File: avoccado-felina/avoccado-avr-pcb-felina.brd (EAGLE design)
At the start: 25 x 25 mm, 61 parts, among them Q1 16MHz, Q2 FET, U2 MCP73831

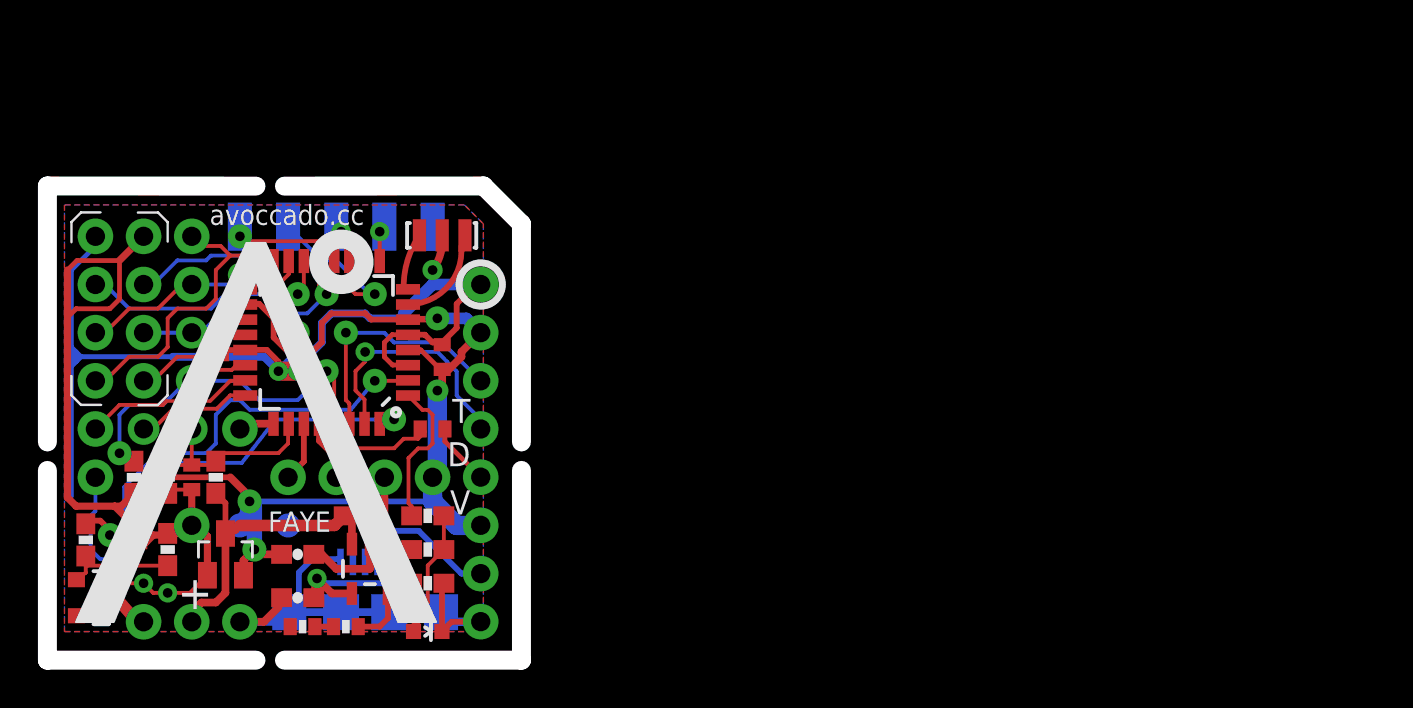
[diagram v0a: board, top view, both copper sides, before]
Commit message: Faye: adjusted Rs, new PCB: Felina
Felina is a larger PCB with the MPU6050 on board instead of a breakout
board.
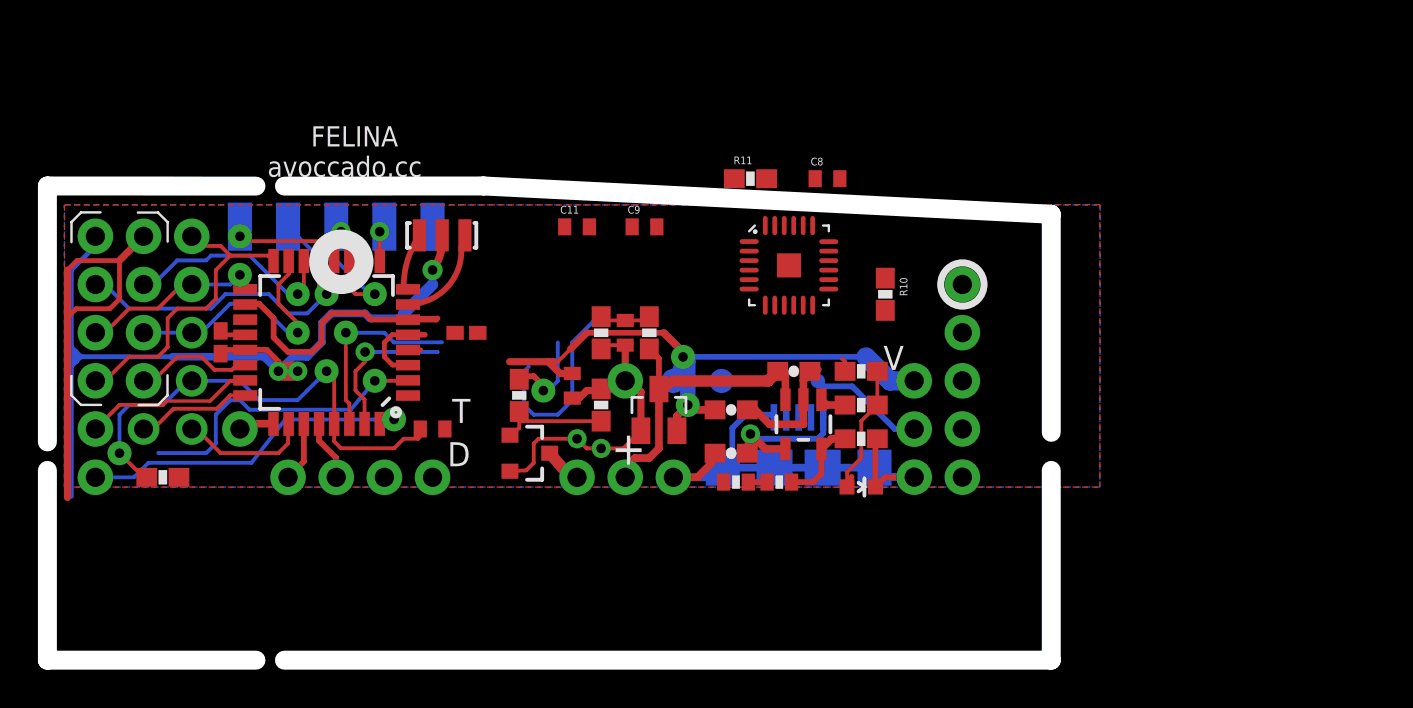
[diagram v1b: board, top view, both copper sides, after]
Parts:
- added C11, C8: 0.1uF, SparkFun:C0402
- added C9: 2.2nF, SparkFun:C0402
- added R10, R11: 10K, SparkFun-Resistors:0603-RES
- added U1: MPU-6000QFN-24, SparkFun-Sensors:QFN-24-TESTING
- C1, C3: device SparkFun:C0402 -> resistor:C0402K
- moved JP10 25.4 mm to (47.8, 9.15)
- moved JP11 25.4 mm to (47.8, 16.8)
- moved JP3 25.4 mm to (47.8, 19.3)
- moved JP8 25.4 mm to (47.8, 14.2)
- moved JP9 25.4 mm to (47.8, 11.7)
- moved C4 24.1 mm to (35.6, 10.4)
- moved C5 24.1 mm to (38.9, 14.7)
- moved C6 24.1 mm to (35.6, 12.7)
- moved JP17 24.1 mm to (45.2, 11.7)
- moved JP18 24.1 mm to (45.2, 14.2)
- moved JP26 24.1 mm to (45.2, 9.15)
- moved R5 24.1 mm to (28.7, 13.0)
- moved R7 24.1 mm to (28.7, 16.8)
- moved C10 24.1 mm to (27.2, 14.0)
- moved C7 24.1 mm to (30.0, 16.8)
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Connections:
- removed net D2: MCU.32, TP2.1
- new net D2-INT: MCU.32, TP2.1, U1.12
- new net N$10: C11.1, U1.8
- new net N$4: R10.1, U1.23
- new net N$5: R11.1, U1.24
- new net N$7: C8.1, U1.10
- new net N$8: C9.1, U1.20
- net 3.3V: now also R10.2, R11.2, U1.13
- net GND: now also C11.2, C8.2, C9.2, U1.1, U1.11, U1.18, U1.9
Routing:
- net D2-INT: track 0.00 -> 28.1 mm, vias 0 -> 1
- net D2: track 26.0 -> 0.00 mm, vias 1 -> 0
- net 3.3V: track 85.0 -> 70.0 mm, vias 4 -> 2
- net GND: track 112.5 -> 103.0 mm
- net D3: track 8.43 -> 1.22 mm
- net TXO: track 13.2 -> 9.05 mm
- net DTR: track 3.33 -> 0.01 mm
- net RXI: track 13.1 -> 10.2 mm
- net D4: track 23.5 -> 21.0 mm
- net RESET: track 25.1 -> 26.2 mm
- net A3: track 10.4 -> 9.84 mm
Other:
- board size 25 x 25 mm -> 52.9 x 25 mm
- board text added: "FELINA"
- board text removed: "FAYE"

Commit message: Felina: rearrange and start to route
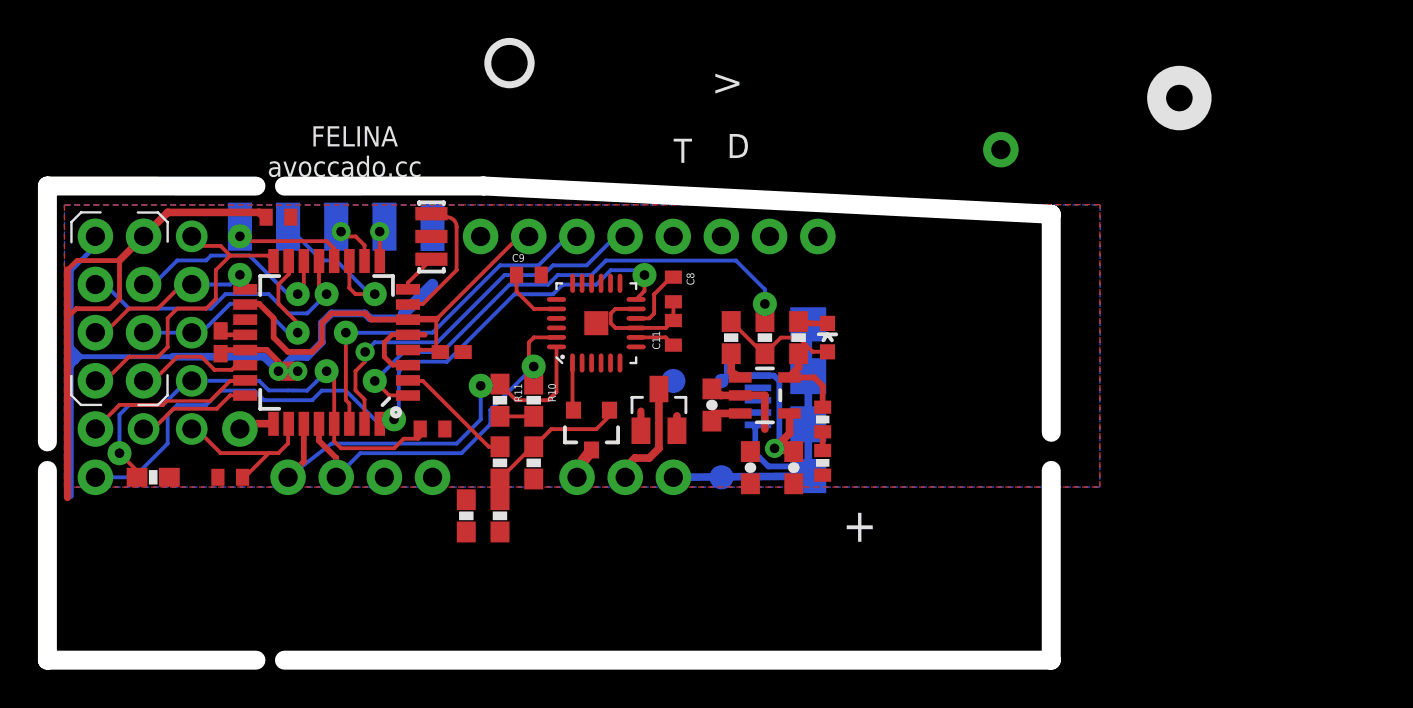
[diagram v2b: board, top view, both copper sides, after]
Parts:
- JP12: value M01PTH -> M01NOSILK-KIT; device SparkFun-Connectors:1X01 -> SparkFun-Connectors:1X01NS-KIT
- moved JP3 25.5 mm to (22.3, 21.8), turned to 90 degrees
- moved JP11 23.4 mm to (24.9, 21.8), turned to 90 degrees
- moved JP6 23.3 mm to (49.8, 26.4)
- moved C7 22.2 mm to (9.14, 9.14), turned to 180 degrees
- moved JP8 21.7 mm to (27.4, 21.8), turned to 90 degrees
- moved JP9 20.5 mm to (30.0, 21.8), turned to 90 degrees
- moved JP10 19.8 mm to (32.5, 21.8), turned to 90 degrees
- moved R10 19.4 mm to (25.1, 13.2)
- moved C10 17.9 mm to (11.7, 22.9), turned to 0 degrees
- moved R11 17.6 mm to (23.4, 13.2), turned to 270 degrees
- moved JP26 14.8 mm to (37.6, 21.8), turned to 90 degrees
- moved R8 13.6 mm to (21.6, 7.11)
- moved JP18 12.7 mm to (35.0, 21.8), turned to 90 degrees
- moved JP17 11.4 mm to (40.1, 21.8), turned to 90 degrees
- moved R7 11.0 mm to (23.4, 7.11)
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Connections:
- removed net N$4: R10.1, U1.23
- removed net N$5: R11.1, U1.24
- net A4: now also R11.1, U1.24
- net A5: now also R10.1, U1.23
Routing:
- net D3: track 1.22 -> 27.6 mm, vias 0 -> 2
- net A4: track 3.17 -> 23.2 mm, vias 0 -> 1
- net A5: track 3.20 -> 21.4 mm, vias 0 -> 1
- net GND: track 103.0 -> 85.7 mm, vias 5 -> 2
- net D4: track 21.0 -> 6.30 mm, vias 2 -> 0
- net 3.3V: track 70.0 -> 57.2 mm, vias 2 -> 0
- net D2-INT: track 28.1 -> 39.8 mm, vias 1 -> 2
- net TXO: track 9.05 -> 20.4 mm
- net RXI: track 10.2 -> 19.2 mm
- net VBAT: track 16.9 -> 7.89 mm
- net 5V: track 16.1 -> 12.0 mm
- net N$7: track 0.00 -> 3.46 mm
- net N$8: track 0.00 -> 3.36 mm
- net N$2: track 4.88 -> 7.22 mm
- net N$10: track 0.00 -> 2.13 mm
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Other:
- board text removed: "A1"
- board text removed: "A3"

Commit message: route 3V3
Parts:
- moved C2 15.9 mm to (33.9, 19.1), turned to 90 degrees
- moved C10 13.4 mm to (24.6, 19.3), turned to 270 degrees
- moved JP18 9.86 mm to (44.7, 23.9)
- moved R7 6.28 mm to (21.8, 13.2), turned to 270 degrees
- moved R8 2.81 mm to (21.8, 9.91)
- moved C9 2.65 mm to (24.1, 17.3), turned to 180 degrees
- moved JP17 2.54 mm to (40.1, 19.3)
- moved JP26 1.52 mm to (36.1, 21.8)
- moved C3 1.04 mm to (21.1, 16.8), turned to 270 degrees
- moved R1 0.25 mm to (23.6, 9.91)
- moved R11 0.25 mm to (23.6, 13.2)
- moved R10 0.25 mm to (25.4, 13.2)
- moved R5 0.25 mm to (25.4, 9.91)
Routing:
- net 3.3V: track 57.2 -> 87.5 mm, vias 0 -> 1
- net RESET: track 25.9 -> 51.9 mm, vias 2 -> 4
- net DTR: track 0.00 -> 2.72 mm
- net A3: track 8.78 -> 11.2 mm, vias 0 -> 1
- net GND: track 85.7 -> 87.9 mm
- net A4: track 23.2 -> 24.7 mm
- net D4: track 6.30 -> 7.82 mm
- net N$8: track 3.36 -> 1.88 mm
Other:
- board size 52.9 x 25 mm -> 42 x 17.4 mm

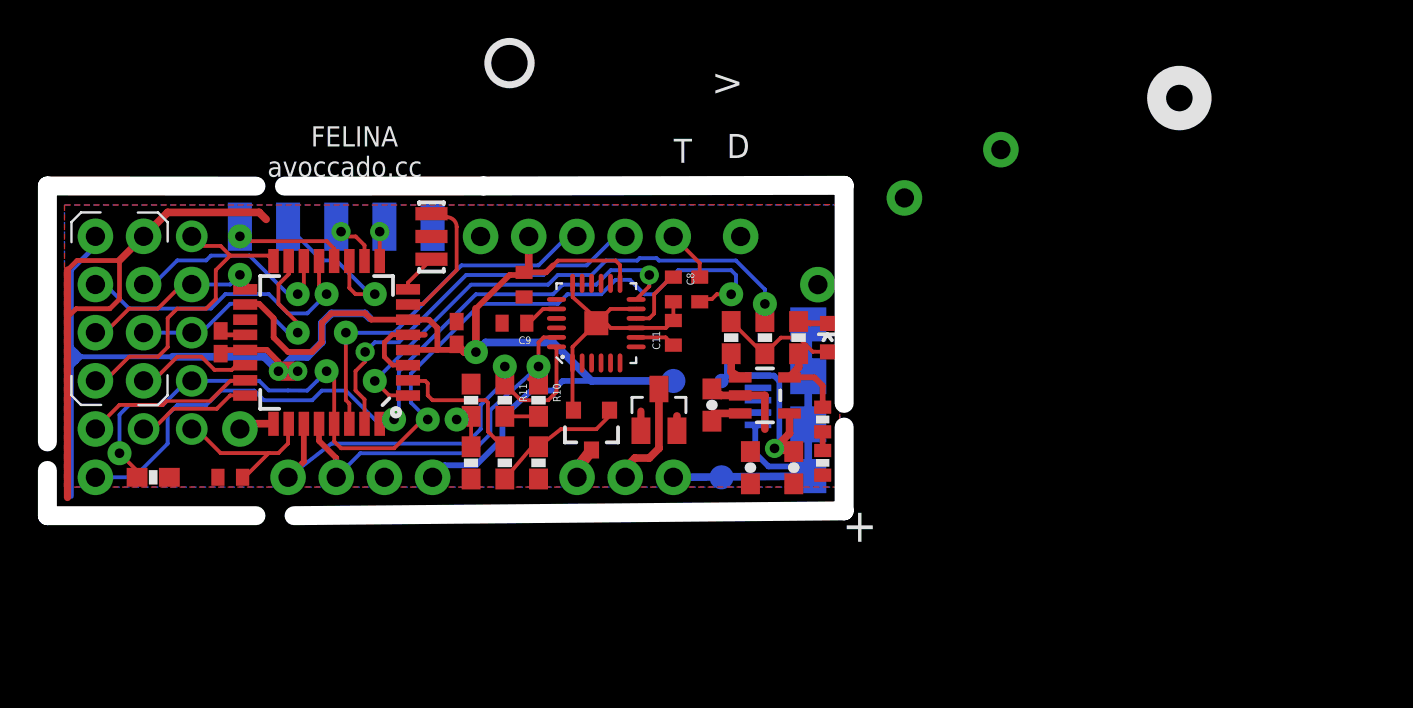
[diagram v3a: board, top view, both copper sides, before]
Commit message: move RST pullup away from bottom left
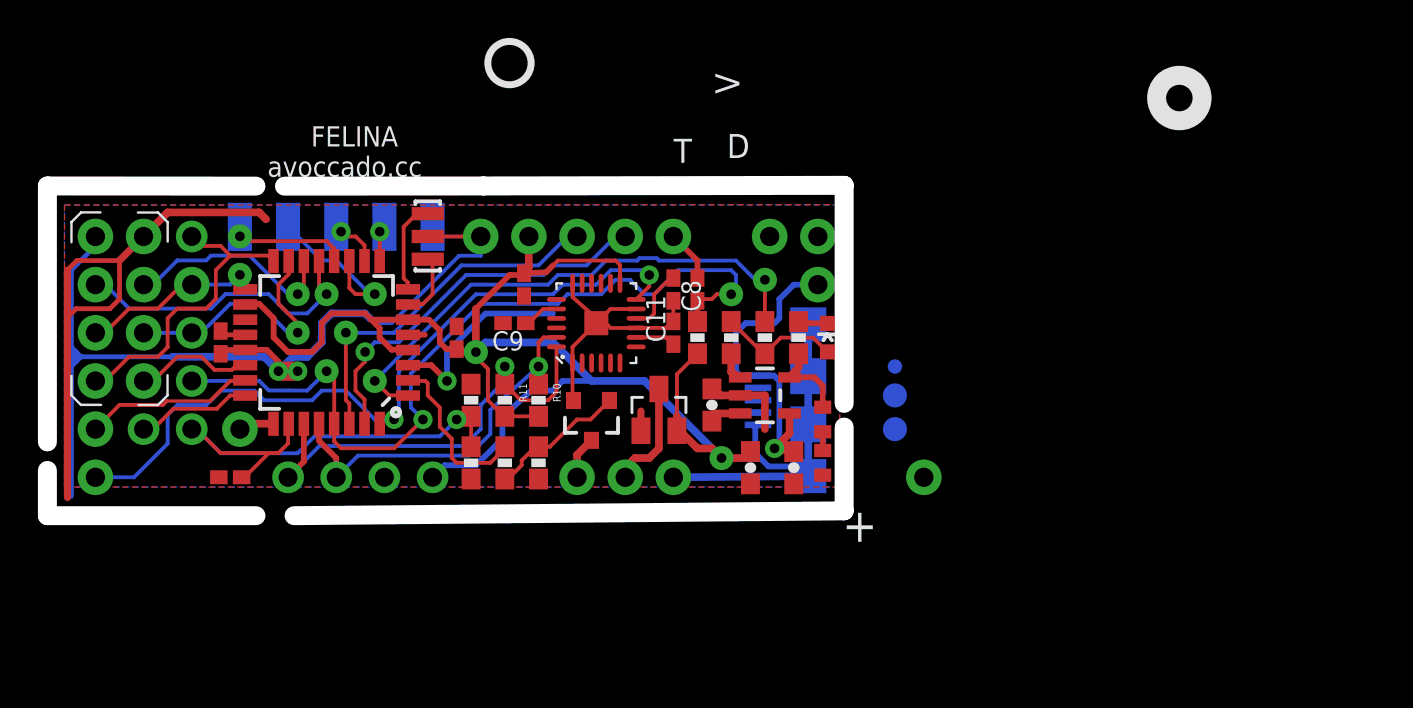
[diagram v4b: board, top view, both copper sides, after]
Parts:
- removed JP4, JP5: M021X02_NO_SILK, SparkFun-Connectors:1X02_NO_SILK
- added JP1, JP16, JP30, JP31: M01NOSILK-KIT, SparkFun-Connectors:1X01NS-KIT
- C10, C11, C2, C7, C8, C9: device SparkFun:C0402 -> rcl:C0402K
- R12, R9: device SparkFun-Resistors:0402-RES -> rcl:R0402
- R3: value RP -> 2K
- R4: value 1K -> 2K
- moved R2 29.6 mm to (33.8, 16.5), turned to 270 degrees
- moved JP18 14.8 mm to (45.7, 9.14)
- moved JP6 13.0 mm to (37.6, 21.8)
- moved TP5 11.7 mm to (44.2, 13.5)
- moved TP3 9.49 mm to (44.2, 11.7)
- moved TP4 9.18 mm to (44.2, 15.0)
- moved JP26 4.07 mm to (40.1, 21.8)
- moved Q2 0.51 mm to (28.2, 12.2)
- moved C3 0.25 mm to (21.1, 16.5)
- moved Q1 0.20 mm to (19.6, 21.8), turned to 270 degrees
- moved C2 0.12 mm to (33.8, 19.1)
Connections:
- net 3.3V: now also JP1.1; no longer JP4.1
- net A4: now also JP31.1; no longer JP5.2
- net A5: now also JP30.1; no longer JP5.1
- net GND: now also JP16.1; no longer JP4.2
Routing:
- net GND: track 87.9 -> 107.7 mm, vias 2 -> 3
- net 3.3V: track 87.5 -> 104.9 mm, vias 1 -> 2
- net A3: track 11.2 -> 26.5 mm
- net RESET: track 51.9 -> 44.0 mm, vias 4 -> 3
- net 5V: track 12.0 -> 17.6 mm
- net N$2: track 7.22 -> 3.47 mm
- net N$1: track 2.10 -> 4.95 mm
- net D4: track 7.82 -> 8.96 mm
- net D3: track 27.7 -> 28.7 mm
- net A5: track 21.0 -> 20.5 mm

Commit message: Vcc and GND routed at bottom
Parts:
- added JP4, JP5: M01NOSILK-KIT, SparkFun-Connectors:1X01NS-KIT
- added TP10: TPTP20R, testpad:TP20R
- moved JP18 16.6 mm to (35.1, 21.8)
- moved JP22 9.35 mm to (14.0, 5.33)
- moved TP3 4.75 mm to (45.5, 16.3)
- moved C7 4.47 mm to (4.70, 8.64), turned to 0 degrees
- moved TP4 4.38 mm to (43.4, 19.3)
- moved JP26 4.07 mm to (44.2, 21.6)
- moved JP17 2.54 mm to (40.1, 21.8)
- moved C10 2.18 mm to (22.9, 18.0), turned to 90 degrees
- moved C3 1.52 mm to (21.1, 18.0)
- moved TP5 1.02 mm to (45.2, 13.5)
- moved C9 0.92 mm to (24.6, 18.0), turned to 90 degrees
- moved Q2 0.57 mm to (27.9, 11.7)
- moved C11 0.25 mm to (32.5, 16.5)
- turned R5 to 270 degrees
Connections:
- net 3.3V: now also JP4.1
- net GND: now also JP5.1
- net VBAT: now also TP10.TP
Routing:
- net GND: track 107.7 -> 187.2 mm, vias 3 -> 6
- net 3.3V: track 104.9 -> 154.1 mm
- net VBAT: track 7.89 -> 14.7 mm
- net RESET: track 44.0 -> 41.4 mm
- net 5V: track 17.6 -> 20.0 mm
- net VIBR: track 2.26 -> 1.65 mm
- net A3: track 26.5 -> 26.7 mm, vias 1 -> 2

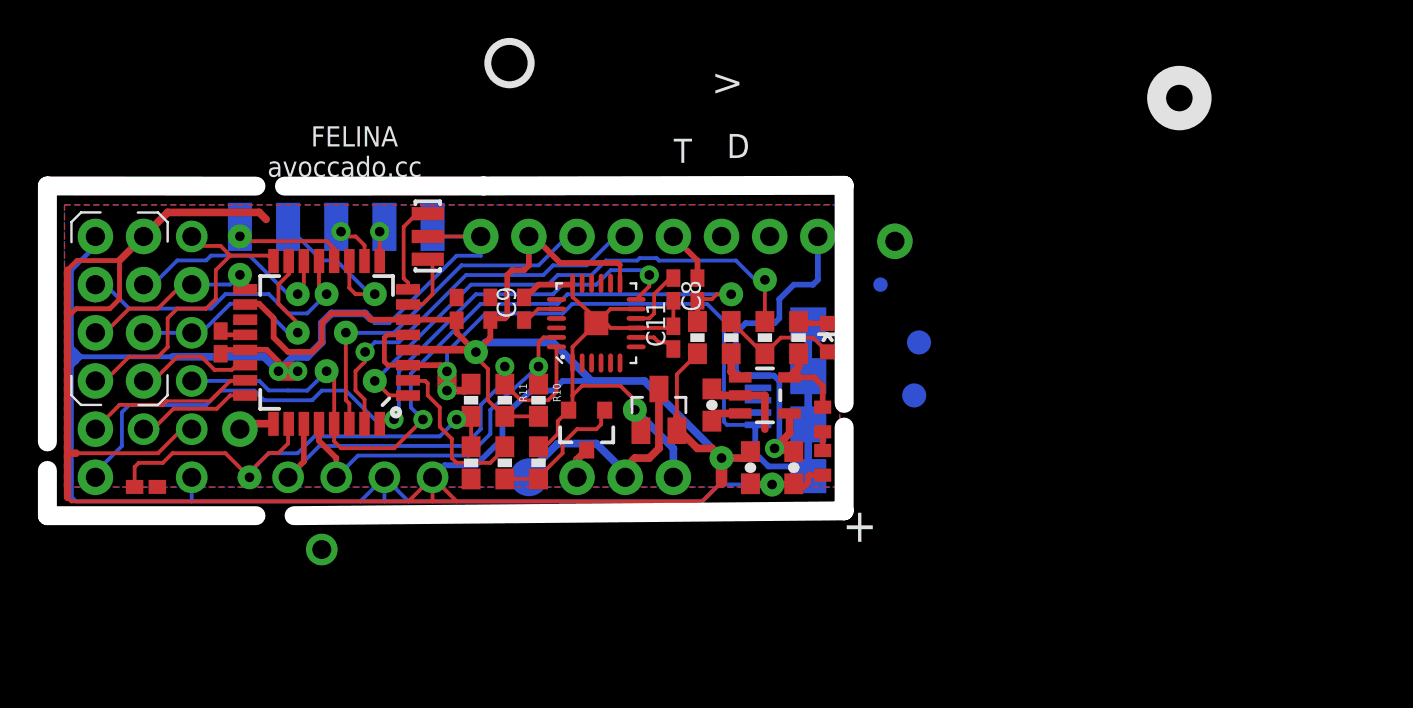
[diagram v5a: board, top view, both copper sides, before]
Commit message: route reset pullup
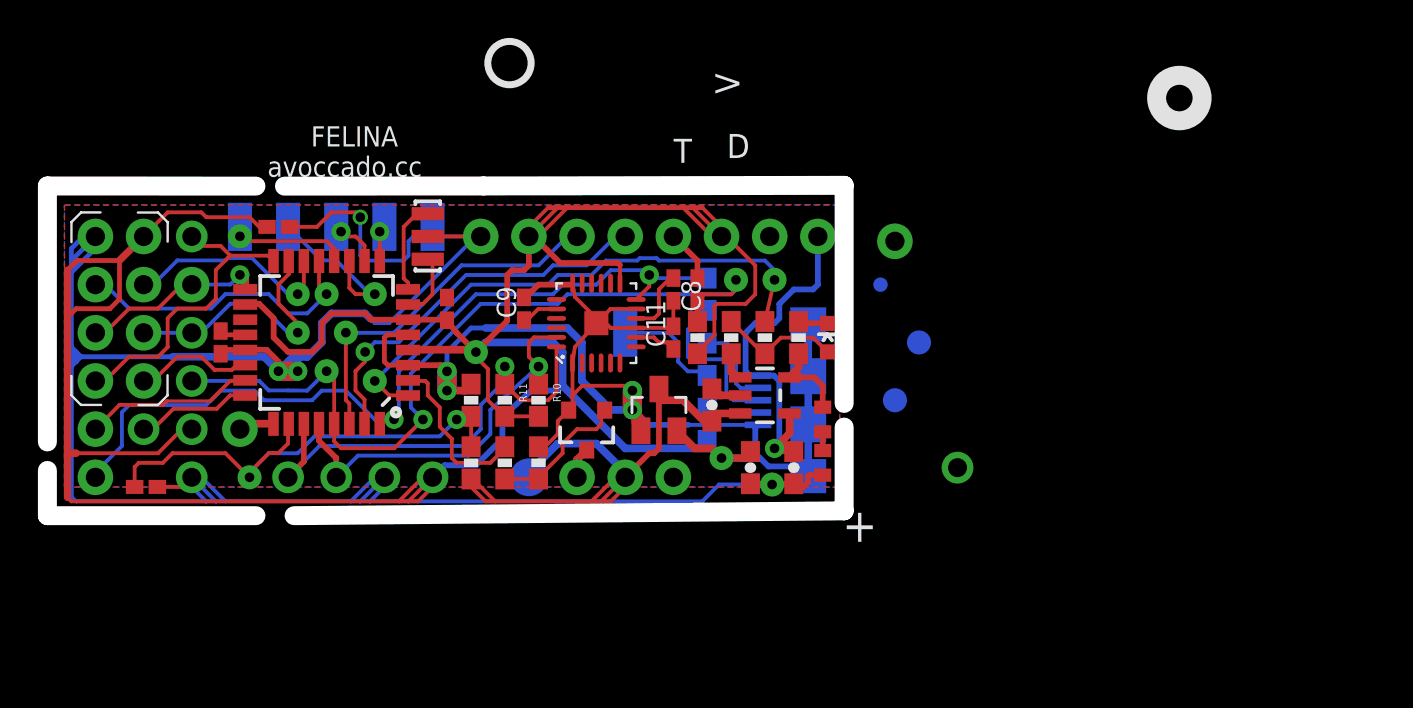
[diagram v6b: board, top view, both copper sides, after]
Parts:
- added R13, R14: 68R, SparkFun-Resistors:0603-RES
- added R15: 2K, SparkFun-Resistors:0603-RES
- added TP11: TEST-POINT2, SparkFun-Passives:PAD.02X.02
- moved LOGO2 35.1 mm to (46.7, 29.5), turned to 270 degrees
- moved JP22 33.8 mm to (47.5, 9.65)
- moved C10 12.0 mm to (11.7, 22.4), turned to 0 degrees
- moved TP5 1.05 mm to (44.2, 13.2)
- moved C3 0.51 mm to (20.6, 18.0)
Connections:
- new net 7-TO-D-: R14.1, R15.1, TP11.P$1
- new net N$4: JP7.D+, R13.2
- new net N$5: JP7.D-, R14.2
- net 3.3V: now also R15.2
- net D2-INT: now also R13.1
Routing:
- net VBAT: track 14.7 -> 32.8 mm
- net GND: track 187.2 -> 203.9 mm, vias 6 -> 8
- net 3.3V: track 154.1 -> 162.9 mm
- net N$4: track 0.00 -> 8.49 mm
- net 7-TO-D-: track 0.00 -> 7.57 mm
- net N$5: track 0.00 -> 4.64 mm
- net D2-INT: track 40.5 -> 43.6 mm
- net RESET: track 41.4 -> 43.1 mm
- net 5V: track 20.0 -> 19.0 mm
- net N$7: track 3.47 -> 4.19 mm
- net A5: track 20.5 -> 21.2 mm
